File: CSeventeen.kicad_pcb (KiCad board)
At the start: 2 copper layers, 320 x 135 mm, 63 parts, among them Q1 2SC1815, Q2 2SC1815, Q3 2SC1815, Q5 2SD880, U1 MOS_7360_TED, U10 NE555, U11 74LS125, U12 74LS02, U13 MOS_6529, U14 74LS139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

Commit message: Add electrolytics
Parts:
- added C16: 10u/25V, Capacitor_THT:CP_Radial_D6.3mm_P2.50mm, F.Cu at (63.3, 100.1)
- added C17: 1u/16V, Capacitor_THT:CP_Radial_D6.3mm_P2.50mm, F.Cu at (72.9, 100.1)
- added C18: 10u/25V, Capacitor_THT:CP_Radial_D6.3mm_P2.50mm, F.Cu at (150.9, 93.1)
- added C19: 10u/25V, Capacitor_THT:CP_Radial_D6.3mm_P2.50mm, F.Cu at (158.7, 93.1)
- added C2: 47u/25V, Capacitor_THT:CP_Radial_D7.5mm_P2.50mm, F.Cu at (310.4, 134.9)
- added C3: 10u/25V, Capacitor_THT:CP_Radial_D6.3mm_P2.50mm, F.Cu at (170.7, 156.2)
- added C31: 10u/25V, Capacitor_THT:CP_Radial_D6.3mm_P2.50mm, F.Cu at (178.1, 101.9)
- added C4: 10u/25V, Capacitor_THT:CP_Radial_D6.3mm_P2.50mm, F.Cu at (170.7, 135.7)
- moved Q3 203.1 mm to (172.2, 101.9), turned to 180 degrees
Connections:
- R11 pad 2: (no net) -> Net-(C31-Pad2)
- R28 pad 1: (no net) -> Net-(C18-Pad2)
- R8 pad 1: (no net) -> Net-(C19-Pad2)

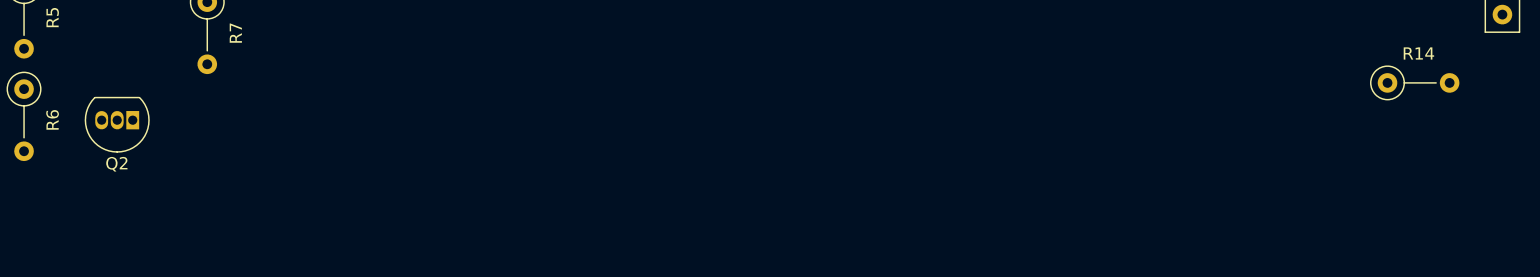
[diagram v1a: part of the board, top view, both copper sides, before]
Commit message: Add pin headers
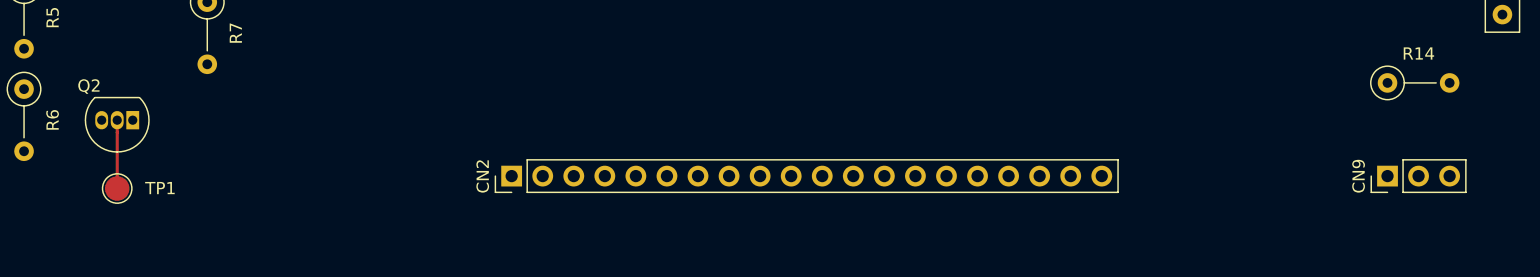
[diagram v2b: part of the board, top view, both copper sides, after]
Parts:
- added CN2: KEYBOARD_HEADER, Connector_PinHeader_2.54mm:PinHeader_1x20_P2.54mm_Vertical, F.Cu at (260.4, 190.2)
- added CN9: LED_CONNECTOR, Connector_PinHeader_2.54mm:PinHeader_1x03_P2.54mm_Vertical, F.Cu at (332.0, 190.2)
- added TP1: CLOCK_TESTPOINT, TestPoint:TestPoint_Pad_D2.0mm, F.Cu at (228.1, 191.3)
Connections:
- R14 pad 2: (no net) -> Net-(CN9-Pad1)
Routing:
- net Net-(Q2-Pad2): track 0.00 -> 5.59 mm

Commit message: Add ceramics
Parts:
- added C1: 100n, Capacitor_THT:C_Disc_D8.0mm_W2.5mm_P5.00mm, F.Cu at (311.4, 124.5)
- added C10: 100n, Capacitor_THT:C_Disc_D8.0mm_W2.5mm_P5.00mm, F.Cu at (91.7, 137.1)
- added C11: 100n, Capacitor_THT:C_Disc_D8.0mm_W2.5mm_P5.00mm, F.Cu at (183.1, 97.7)
- added C12: 22p, Capacitor_THT:C_Disc_D8.0mm_W2.5mm_P5.00mm, F.Cu at (170.7, 174.5)
- added C13: 220p, Capacitor_THT:C_Disc_D8.0mm_W2.5mm_P5.00mm, F.Cu at (200.9, 184.7)
- added C14: 150p, Capacitor_THT:C_Disc_D8.0mm_W2.5mm_P5.00mm, F.Cu at (205.9, 190.0)
- added C15: 10p, Capacitor_THT:C_Disc_D8.0mm_W2.5mm_P5.00mm, F.Cu at (225.8, 179.8)
- added C20: 10n, Capacitor_THT:C_Disc_D8.0mm_W2.5mm_P5.00mm, F.Cu at (158.7, 105.7)
- added C200: 220n, Capacitor_THT:C_Disc_D8.0mm_W2.5mm_P5.00mm, F.Cu at (353.3, 86.1)
- added C21: 100n, Capacitor_THT:C_Disc_D8.0mm_W2.5mm_P5.00mm, F.Cu at (170.7, 169.9)
- added C22: 100n, Capacitor_THT:C_Disc_D8.0mm_W2.5mm_P5.00mm, F.Cu at (178.1, 133.2)
- added C23: 470p, Capacitor_THT:C_Disc_D8.0mm_W2.5mm_P5.00mm, F.Cu at (109.2, 77.7)
- added C24: 470p, Capacitor_THT:C_Disc_D8.0mm_W2.5mm_P5.00mm, F.Cu at (109.2, 88.6)
- added C25: 470p, Capacitor_THT:C_Disc_D8.0mm_W2.5mm_P5.00mm, F.Cu at (109.2, 81.5)
- added C26: 100n, Capacitor_THT:C_Disc_D8.0mm_W2.5mm_P5.00mm, F.Cu at (109.2, 73.2)
- added C28: 100n, Capacitor_THT:C_Disc_D8.0mm_W2.5mm_P5.00mm, F.Cu at (91.7, 117.3)
- added C30: 100n, Capacitor_THT:C_Disc_D8.0mm_W2.5mm_P5.00mm, F.Cu at (123.4, 114.0)
- added C32: 100p, Capacitor_THT:C_Disc_D8.0mm_W2.5mm_P5.00mm, F.Cu at (240.5, 183.2)
- added C33: 100n, Capacitor_THT:C_Disc_D8.0mm_W2.5mm_P5.00mm, F.Cu at (250.2, 159.6)
- added C34: 100n, Capacitor_THT:C_Disc_D8.0mm_W2.5mm_P5.00mm, F.Cu at (100.1, 94.3)
- added C5: 100n, Capacitor_THT:C_Disc_D8.0mm_W2.5mm_P5.00mm, F.Cu at (126.0, 182.4)
- added C6: 100n, Capacitor_THT:C_Disc_D8.0mm_W2.5mm_P5.00mm, F.Cu at (126.0, 158.8)
- added C7: 220n, Capacitor_THT:C_Disc_D8.0mm_W2.5mm_P5.00mm, F.Cu at (91.7, 162.6)
- added C8: 220n, Capacitor_THT:C_Disc_D8.0mm_W2.5mm_P5.00mm, F.Cu at (91.7, 181.9)
- moved R23 5.08 mm to (163.1, 100.6), turned to 270 degrees
- moved C31 0.57 mm to (177.8, 101.3)
- moved R5 0.25 mm to (220.7, 174.8)
- moved R6 0.25 mm to (220.7, 183.1)
- moved R3 0.13 mm to (215.6, 174.8)
- moved R4 0.13 mm to (215.6, 183.1)
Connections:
- R29 pad 2: (no net) -> Net-(C24-Pad2)
- U2 pad 26: (no net) -> p4
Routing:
- net Net-(Q2-Pad2): track 5.59 -> 0.00 mm
